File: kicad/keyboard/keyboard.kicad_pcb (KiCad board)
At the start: 2 copper layers, 18 parts, among them P1 CONN03, P2 CONN06, P3 CONN06, P4 CONN06, P5 CONN08, P6 CONN08, U1 ATmega328, U2 MAX7219, Y1 Crystal

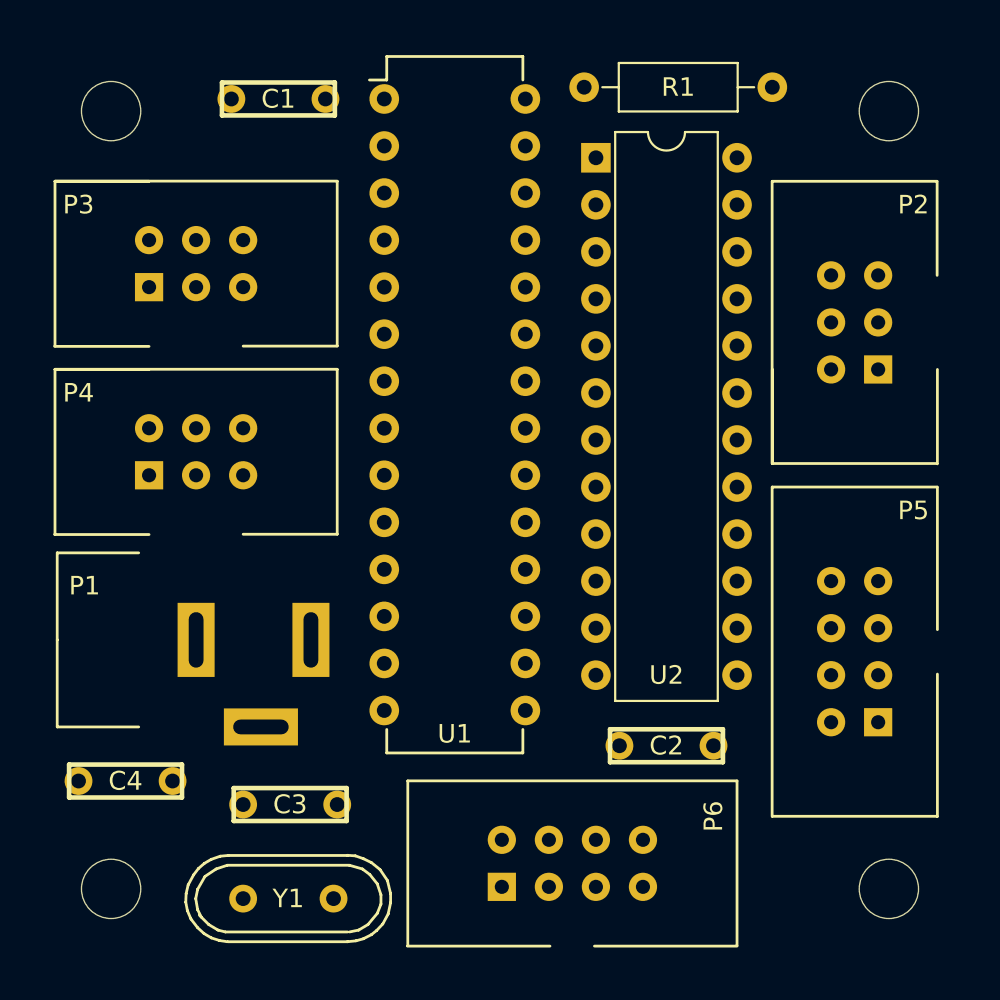
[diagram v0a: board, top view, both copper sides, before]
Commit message: Add the tracks to the Keypad Controller PCB
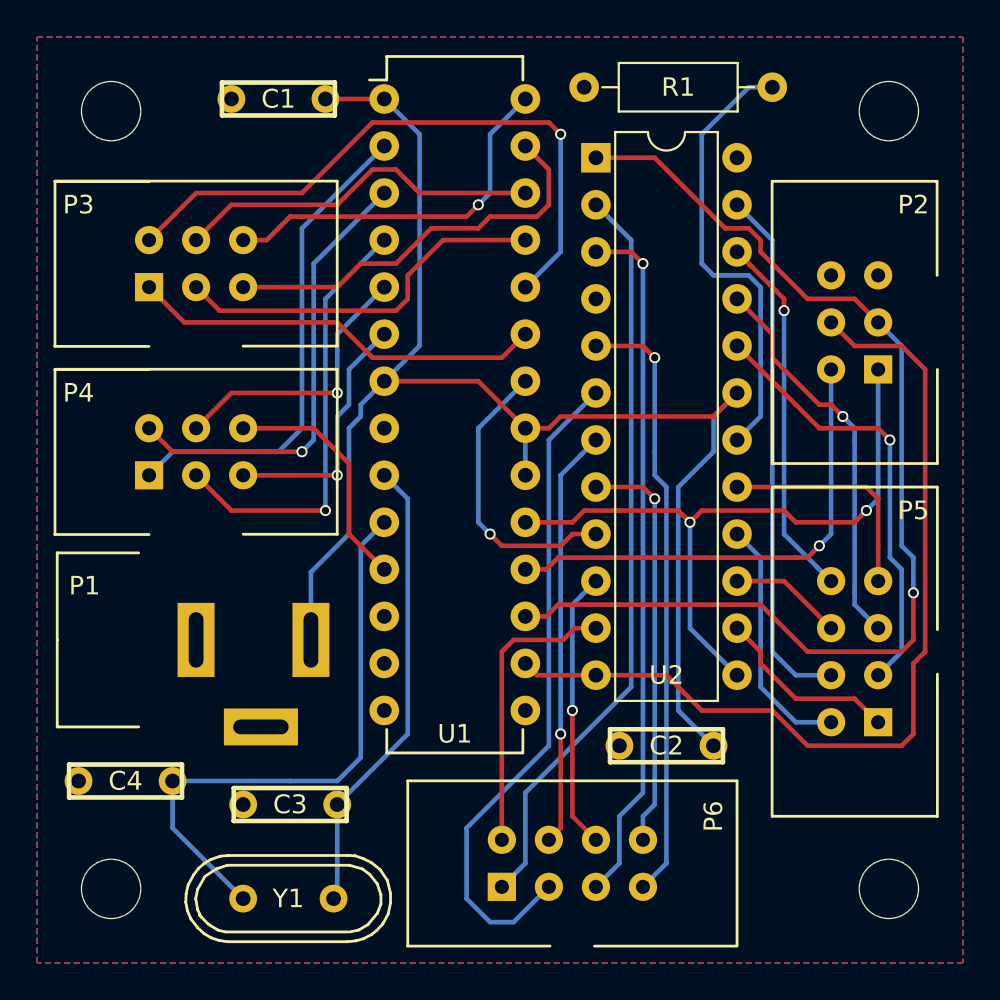
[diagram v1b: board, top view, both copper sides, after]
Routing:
- net VCC: track 0.00 -> 80.2 mm
- net Net-(P2-Pad3): track 0.00 -> 59.8 mm, vias 0 -> 1
- net Net-(P2-Pad4): track 0.00 -> 49.1 mm
- net Net-(P6-Pad1): track 0.00 -> 40.5 mm
- net Net-(P6-Pad5): track 0.00 -> 37.5 mm, vias 0 -> 1
- net Net-(P2-Pad1): track 0.00 -> 36.9 mm, vias 0 -> 2
- net Net-(P6-Pad3): track 0.00 -> 36.0 mm
- net Net-(P3-Pad2): track 0.00 -> 34.2 mm, vias 0 -> 1
- net Net-(P6-Pad7): track 0.00 -> 32.8 mm, vias 0 -> 1
- net Net-(C4-Pad1): track 0.00 -> 31.8 mm
- net Net-(P5-Pad4): track 0.00 -> 28.6 mm
- net Net-(P4-Pad1): track 0.00 -> 26.4 mm
- net Net-(P2-Pad2): track 0.00 -> 26.2 mm, vias 0 -> 1
- net Net-(C3-Pad1): track 0.00 -> 25.0 mm
- net Net-(P4-Pad2): track 0.00 -> 24.6 mm, vias 0 -> 1
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- added copper zone on B.Cu, net GND
- added copper zone on F.Cu, net GND

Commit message: Introduce a DAV signal in the Keypad Controller board
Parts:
- U1: value ATmega328 -> atmega328
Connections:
- P2 pad 5: GND -> Net-(P2-Pad5)
- U1 pad 15: (no net) -> Net-(P2-Pad5)
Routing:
- net Net-(P2-Pad5): track 0.00 -> 49.9 mm
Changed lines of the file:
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@@
     (thickness 1.6)
     (drawings 4)
-    (tracks 285)
+    (tracks 297)
     (zones 0)
     (modules 18)
-    (nets 38)
+    (nets 39)
   )
   (page A4)
@@
   (net 36 "Net-(R1-Pad2)")
   (net 37 "Net-(C4-Pad1)")
+  (net 38 "Net-(P2-Pad5)")
   (net_class Default "Esta es la clase de red por defecto."
     (clearance 0.2)
@@
     (add_net "Net-(P2-Pad3)")
     (add_net "Net-(P2-Pad4)")
+    (add_net "Net-(P2-Pad5)")
     (add_net "Net-(P3-Pad1)")
     (add_net "Net-(P3-Pad2)")
@@
       (net 7 "Net-(P2-Pad4)"))
     (pad 5 thru_hole circle (at 0 5.08 180) (size 1.524 1.524) (drill 0.762) (layers *.Cu *.Mask F.SilkS)
-      (net 2 GND))
+      (net 38 "Net-(P2-Pad5)"))
     (pad 6 thru_hole circle (at 2.54 5.08 180) (size 1.524 1.524) (drill 0.762) (layers *.Cu *.Mask F.SilkS)
       (net 2 GND))
@@
       (effects (font (size 1 1) (thickness 0.15)))
     )
-    (fp_text value ATmega328 (at 3.81 16.51 90) (layer F.Fab)
+    (fp_text value atmega328 (at 3.81 16.51 90) (layer F.Fab)
       (effects (font (size 1 1) (thickness 0.15)))
     )
@@
     (pad 13 thru_hole oval (at 0 30.48) (size 1.6 1.6) (drill 0.8) (layers *.Cu *.Mask))
     (pad 14 thru_hole oval (at 0 33.02) (size 1.6 1.6) (drill 0.8) (layers *.Cu *.Mask))
-    (pad 15 thru_hole oval (at 7.62 33.02) (size 1.6 1.6) (drill 0.8) (layers *.Cu *.Mask))
+    (pad 15 thru_hole oval (at 7.62 33.02) (size 1.6 1.6) (drill 0.8) (layers *.Cu *.Mask)
+      (net 38 "Net-(P2-Pad5)"))
     (pad 16 thru_hole oval (at 7.62 30.48) (size 1.6 1.6) (drill 0.8) (layers *.Cu *.Mask)
       (net 7 "Net-(P2-Pad4)"))
@@
   (via (at 172.72 102.235) (size 0.6) (drill 0.4) (layers F.Cu B.Cu) (net 32))
   (segment (start 170.18 101.6) (end 172.085 101.6) (width 0.25) (layer F.Cu) (net 32))
-  (segment (start 168.91 126.365) (end 168.91 132.08) (width 0.25) (layer F.Cu) (net 33))
+  (segment (start 168.91 127) (end 168.91 120.65) (width 0.25) (layer B.Cu) (net 33))
+  (segment (start 168.91 120.65) (end 169.380001 120.179999) (width 0.25) (layer B.Cu) (net 33))
+  (segment (start 169.380001 120.179999) (end 170.18 119.38) (width 0.25) (layer B.Cu) (net 33))
+  (segment (start 168.91 132.08) (end 168.91 127) (width 0.25) (layer F.Cu) (net 33))
+  (via (at 168.91 127) (size 0.6) (drill 0.4) (layers F.Cu B.Cu) (net 33))
   (segment (start 168.91 132.08) (end 170.18 133.35) (width 0.25) (layer F.Cu) (net 33))
-  (segment (start 169.380001 120.179999) (end 168.91 120.65) (width 0.25) (layer B.Cu) (net 33))
-  (segment (start 168.91 120.65) (end 168.91 126.365) (width 0.25) (layer B.Cu) (net 33))
-  (via (at 168.91 126.365) (size 0.6) (drill 0.4) (layers F.Cu B.Cu) (net 33))
-  (segment (start 170.18 119.38) (end 169.380001 120.179999) (width 0.25) (layer B.Cu) (net 33))
   (segment (start 173.355 113.665) (end 173.355 112.395) (width 0.25) (layer B.Cu) (net 34))
   (segment (start 173.99 134.62) (end 173.99 114.3) (width 0.25) (layer B.Cu) (net 34))
@@
   (segment (start 147.32 130.175) (end 147.32 132.715) (width 0.25) (layer B.Cu) (net 37))
   (segment (start 147.32 132.715) (end 151.13 136.525) (width 0.25) (layer B.Cu) (net 37))
+  (segment (start 166.37 126.365) (end 174.625 126.365) (width 0.25) (layer F.Cu) (net 38))
+  (segment (start 174.625 126.365) (end 175.26 127) (width 0.25) (layer F.Cu) (net 38))
+  (segment (start 175.26 127) (end 179.07 127) (width 0.25) (layer F.Cu) (net 38))
+  (segment (start 187.96 124.46) (end 188.595 123.825) (width 0.25) (layer F.Cu) (net 38))
+  (segment (start 179.07 127) (end 180.975 128.905) (width 0.25) (layer F.Cu) (net 38))
+  (segment (start 180.975 128.905) (end 187.325 128.905) (width 0.25) (layer F.Cu) (net 38))
+  (segment (start 187.325 128.905) (end 187.96 128.27) (width 0.25) (layer F.Cu) (net 38))
+  (segment (start 187.96 128.27) (end 187.96 124.46) (width 0.25) (layer F.Cu) (net 38))
+  (segment (start 188.595 123.825) (end 188.595 107.315) (width 0.25) (layer F.Cu) (net 38))
+  (segment (start 188.595 107.315) (end 187.325 106.045) (width 0.25) (layer F.Cu) (net 38))
+  (segment (start 187.325 106.045) (end 187.325 104.775) (width 0.25) (layer F.Cu) (net 38))
+  (segment (start 187.325 104.775) (end 185.42 102.87) (width 0.25) (layer F.Cu) (net 38))
   (zone (net 2) (net_name GND) (layer F.Cu) (hatch edge 0.508)
     (connect_pads (clearance 0.508))

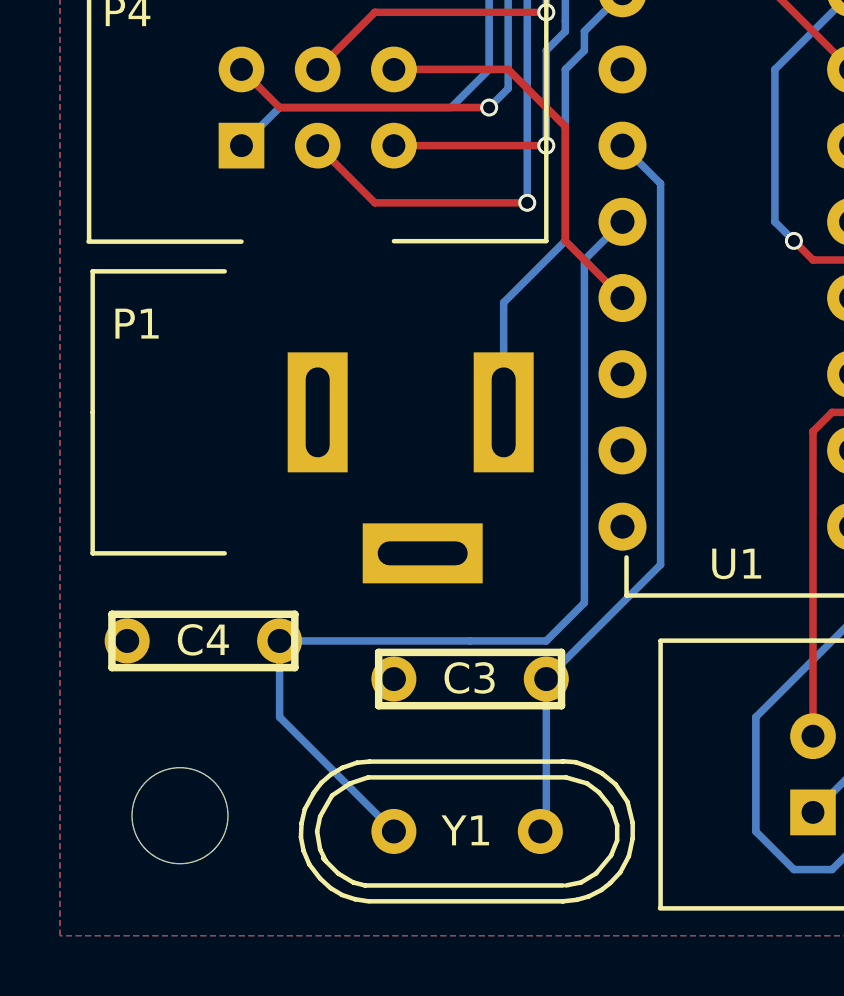
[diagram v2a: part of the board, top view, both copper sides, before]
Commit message: Better alignment of oscillator capacitors in Keypad PCB
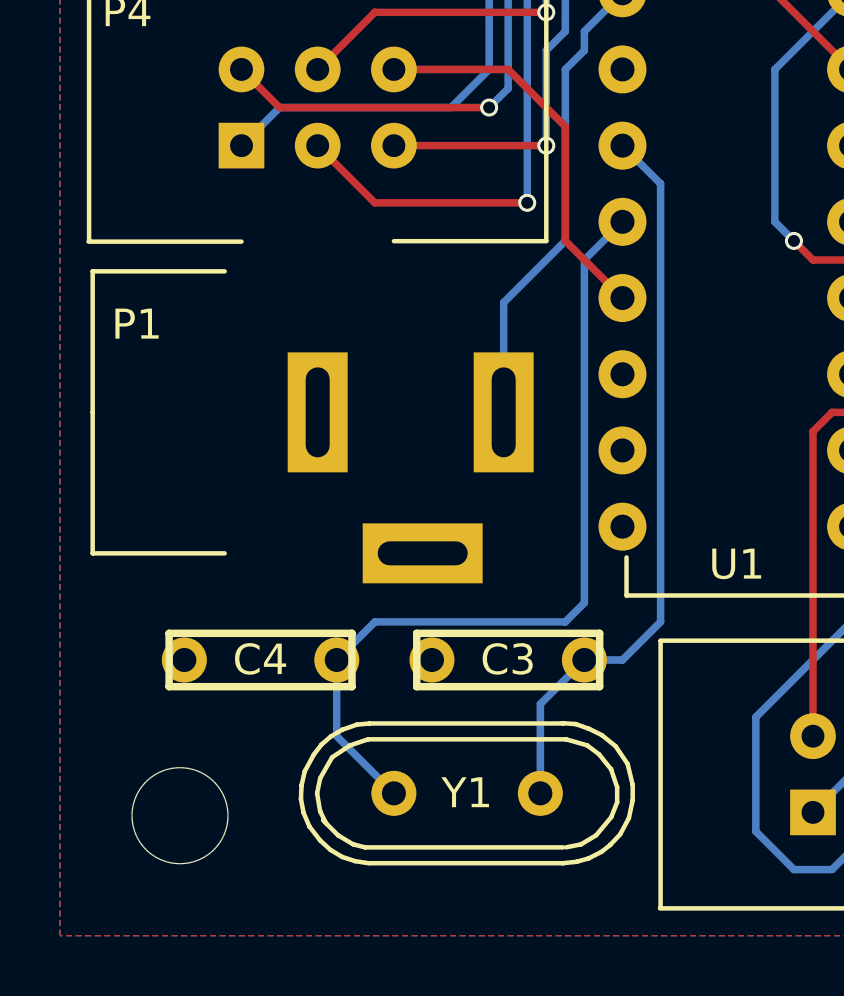
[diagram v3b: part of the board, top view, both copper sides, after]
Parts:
- moved C4 2.01 mm to (146.7, 130.8)
- moved C3 1.42 mm to (154.9, 130.8)
- moved Y1 1.27 mm to (153.6, 135.3)
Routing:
- net Net-(C4-Pad1): track 31.8 -> 27.5 mm
- net Net-(C3-Pad1): track 25.0 -> 24.5 mm
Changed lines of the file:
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@@
     (thickness 1.6)
     (drawings 4)
-    (tracks 297)
+    (tracks 298)
     (zones 0)
     (modules 18)
@@
     (mod_text_size 1 1)
     (mod_text_width 0.15)
-    (pad_size 1.524 1.524)
-    (pad_drill 0.762)
+    (pad_size 1.6 1.6)
+    (pad_drill 0.8)
     (pad_to_mask_clearance 0.2)
     (aux_axis_origin 0 0)
@@
   )
   (module avionica:Disc_capacitor (layer F.Cu)
-    (at 153.67 131.445 180)
+    (at 154.94 130.81 180)
     (descr "6mm disc ceramic capacitor")
     (tags C)
@@
   )
   (module avionica:Crystal (layer F.Cu)
-    (at 153.57094 136.525 180)
+    (at 153.57094 135.255 180)
     (fp_text reference Y1 (at 0 0 180) (layer F.SilkS)
       (effects (font (size 1 1) (thickness 0.15)))
@@
   )
   (module avionica:Disc_capacitor (layer F.Cu)
-    (at 144.78 130.175 180)
+    (at 146.685 130.81 180)
     (descr "6mm disc ceramic capacitor")
     (tags C)
@@
   (segment (start 169.04863 116.84) (end 168.91 116.84) (width 0.25) (layer F.Cu) (net 2))
   (segment (start 170.18 116.84) (end 169.04863 116.84) (width 0.25) (layer F.Cu) (net 2))
-  (segment (start 156.21 131.445) (end 160.02 127.635) (width 0.25) (layer B.Cu) (net 3))
-  (segment (start 160.02 127.635) (end 160.02 114.935) (width 0.25) (layer B.Cu) (net 3))
+  (segment (start 157.48 130.81) (end 156.01188 132.27812) (width 0.25) (layer B.Cu) (net 3))
+  (segment (start 156.01188 132.27812) (end 156.01188 135.255) (width 0.25) (layer B.Cu) (net 3))
+  (segment (start 158.75 130.81) (end 157.48 130.81) (width 0.25) (layer B.Cu) (net 3))
+  (segment (start 160.02 129.54) (end 158.75 130.81) (width 0.25) (layer B.Cu) (net 3))
+  (segment (start 160.02 129.54) (end 160.02 114.935) (width 0.25) (layer B.Cu) (net 3))
   (segment (start 160.02 114.935) (end 158.75 113.665) (width 0.25) (layer B.Cu) (net 3))
-  (segment (start 156.21 131.445) (end 156.21 136.32688) (width 0.25) (layer B.Cu) (net 3))
-  (segment (start 156.21 136.32688) (end 156.01188 136.525) (width 0.25) (layer B.Cu) (net 3))
   (segment (start 185.42 114.935) (end 185.42 107.95) (width 0.25) (layer B.Cu) (net 4))
   (segment (start 184.785 115.57) (end 185.42 114.935) (width 0.25) (layer B.Cu) (net 4))
@@
   (segment (start 179.07 103.505) (end 179.07 110.49) (width 0.25) (layer B.Cu) (net 36))
   (segment (start 179.07 110.49) (end 177.8 111.76) (width 0.25) (layer B.Cu) (net 36))
+  (segment (start 149.225 130.81) (end 149.225 133.35) (width 0.25) (layer B.Cu) (net 37))
+  (segment (start 149.225 133.35) (end 151.13 135.255) (width 0.25) (layer B.Cu) (net 37))
   (segment (start 158.75 116.205) (end 157.48 117.475) (width 0.25) (layer B.Cu) (net 37))
   (segment (start 157.48 117.475) (end 157.48 128.905) (width 0.25) (layer B.Cu) (net 37))
-  (segment (start 157.48 128.905) (end 156.21 130.175) (width 0.25) (layer B.Cu) (net 37))
-  (segment (start 156.21 130.175) (end 153.67 130.175) (width 0.25) (layer B.Cu) (net 37))
-  (segment (start 153.67 130.175) (end 147.32 130.175) (width 0.25) (layer B.Cu) (net 37))
-  (segment (start 147.32 130.175) (end 147.32 132.715) (width 0.25) (layer B.Cu) (net 37))
-  (segment (start 147.32 132.715) (end 151.13 136.525) (width 0.25) (layer B.Cu) (net 37))
+  (segment (start 157.48 128.905) (end 156.845 129.54) (width 0.25) (layer B.Cu) (net 37))
+  (segment (start 156.845 129.54) (end 150.495 129.54) (width 0.25) (layer B.Cu) (net 37))
+  (segment (start 150.495 129.54) (end 149.225 130.81) (width 0.25) (layer B.Cu) (net 37))
   (segment (start 166.37 126.365) (end 174.625 126.365) (width 0.25) (layer F.Cu) (net 38))
   (segment (start 174.625 126.365) (end 175.26 127) (width 0.25) (layer F.Cu) (net 38))

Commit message: Replace 2x6p IDC connectors by a single 12p in Keypad Controller board
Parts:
- removed P4: CONN06, avionica:idc-6p
- P3: value CONN06 -> CONN12; footprint avionica:idc-6p -> avionica:idc-12p
- moved P3 6.75 mm to (151.1, 99.1), turned to 0 degrees
- moved C1 1.27 mm to (153.0, 92.1)
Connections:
- U1 pad 11: Net-(P4-Pad6) -> Net-(P3-Pad12)
- U1 pad 2: Net-(P4-Pad1) -> Net-(P3-Pad7)
- U1 pad 3: Net-(P4-Pad2) -> Net-(P3-Pad8)
- U1 pad 4: Net-(P4-Pad3) -> Net-(P3-Pad9)
- U1 pad 5: Net-(P4-Pad4) -> Net-(P3-Pad10)
- U1 pad 6: Net-(P4-Pad5) -> Net-(P3-Pad11)
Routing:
- net Net-(P4-Pad1): track 26.4 -> 0.00 mm
- net Net-(P4-Pad2): track 24.6 -> 0.00 mm, vias 1 -> 0
- net Net-(P4-Pad3): track 23.7 -> 0.00 mm, vias 1 -> 0
- net Net-(P3-Pad7): track 0.00 -> 16.9 mm
- net Net-(P4-Pad4): track 15.2 -> 0.00 mm, vias 1 -> 0
- net Net-(P4-Pad5): track 13.8 -> 0.00 mm, vias 1 -> 0
- net Net-(P4-Pad6): track 13.0 -> 0.00 mm
- net Net-(P3-Pad9): track 0.00 -> 12.5 mm
- net Net-(P3-Pad8): track 0.00 -> 10.4 mm
- net Net-(P3-Pad11): track 0.00 -> 9.99 mm
- net Net-(P3-Pad12): track 0.00 -> 9.09 mm
- net Net-(P3-Pad10): track 0.00 -> 8.56 mm
- net Net-(P3-Pad2): track 34.2 -> 25.8 mm
- net Net-(P3-Pad1): track 22.4 -> 27.2 mm
- net Net-(P3-Pad4): track 19.9 -> 15.1 mm
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
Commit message: Replace 2x8p IDC connectors by a single 16p in Keypad Controller board
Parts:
- removed P5, P6: CONN08, avionica:idc-8p
- added P4: CONN16, avionica:idc-16p, F.Cu at (185.4, 122.6)
- moved P2 33.1 mm to (167.6, 135.9), turned to 90 degrees
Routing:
- net Net-(P2-Pad4): track 49.1 -> 13.0 mm
- net Net-(P2-Pad5): track 49.9 -> 14.8 mm
- net Net-(P4-Pad13): track 37.5 -> 18.0 mm, vias 1 -> 0
- net Net-(P4-Pad11): track 36.0 -> 16.6 mm
- net Net-(P4-Pad14): track 15.0 -> 32.1 mm
- net Net-(P2-Pad3): track 59.8 -> 43.6 mm, vias 1 -> 0
- net Net-(P4-Pad15): track 32.8 -> 20.1 mm
- net Net-(P4-Pad9): track 40.5 -> 28.8 mm, vias 0 -> 1
- net Net-(P4-Pad16): track 22.1 -> 31.6 mm, vias 1 -> 0
- net Net-(P2-Pad2): track 26.2 -> 16.9 mm, vias 1 -> 0
- net Net-(P4-Pad12): track 22.6 -> 14.0 mm, vias 1 -> 0
- net Net-(P4-Pad8): track 21.0 -> 16.2 mm
- net Net-(P4-Pad3): track 23.8 -> 19.1 mm
- net Net-(P4-Pad4): track 28.6 -> 24.2 mm
- net Net-(P4-Pad7): track 12.3 -> 8.41 mm
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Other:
- board text added: "Avionica data"
- board text added: "Keypad matrix"
- board text added: "LED matrix"
- board text added: "PWR 5V"
